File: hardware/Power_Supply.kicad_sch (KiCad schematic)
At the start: 74 parts, among them U26 LTC3122HMSE#PBF, U27 LTC3115IDHD-2#WPBF, U28 NCP1117-3.3_SOT223, U29 NCP1117-12_SOT223, U30 LM2990SX-12

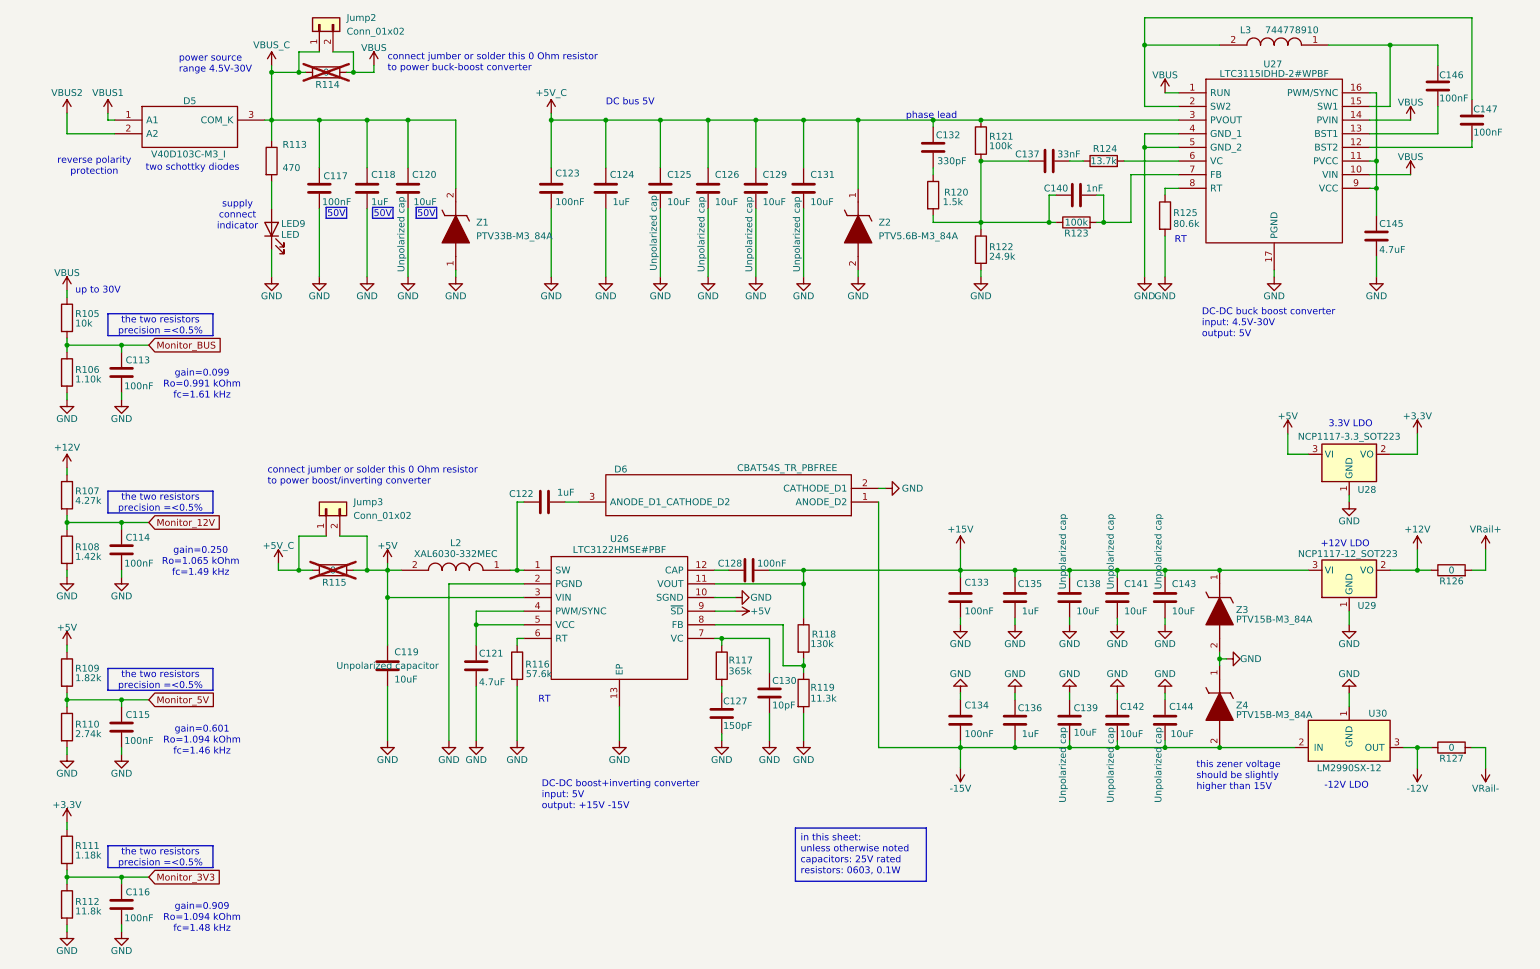
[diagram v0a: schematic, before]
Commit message: BOM for all capacitors and resistors is added correctly to the schematic
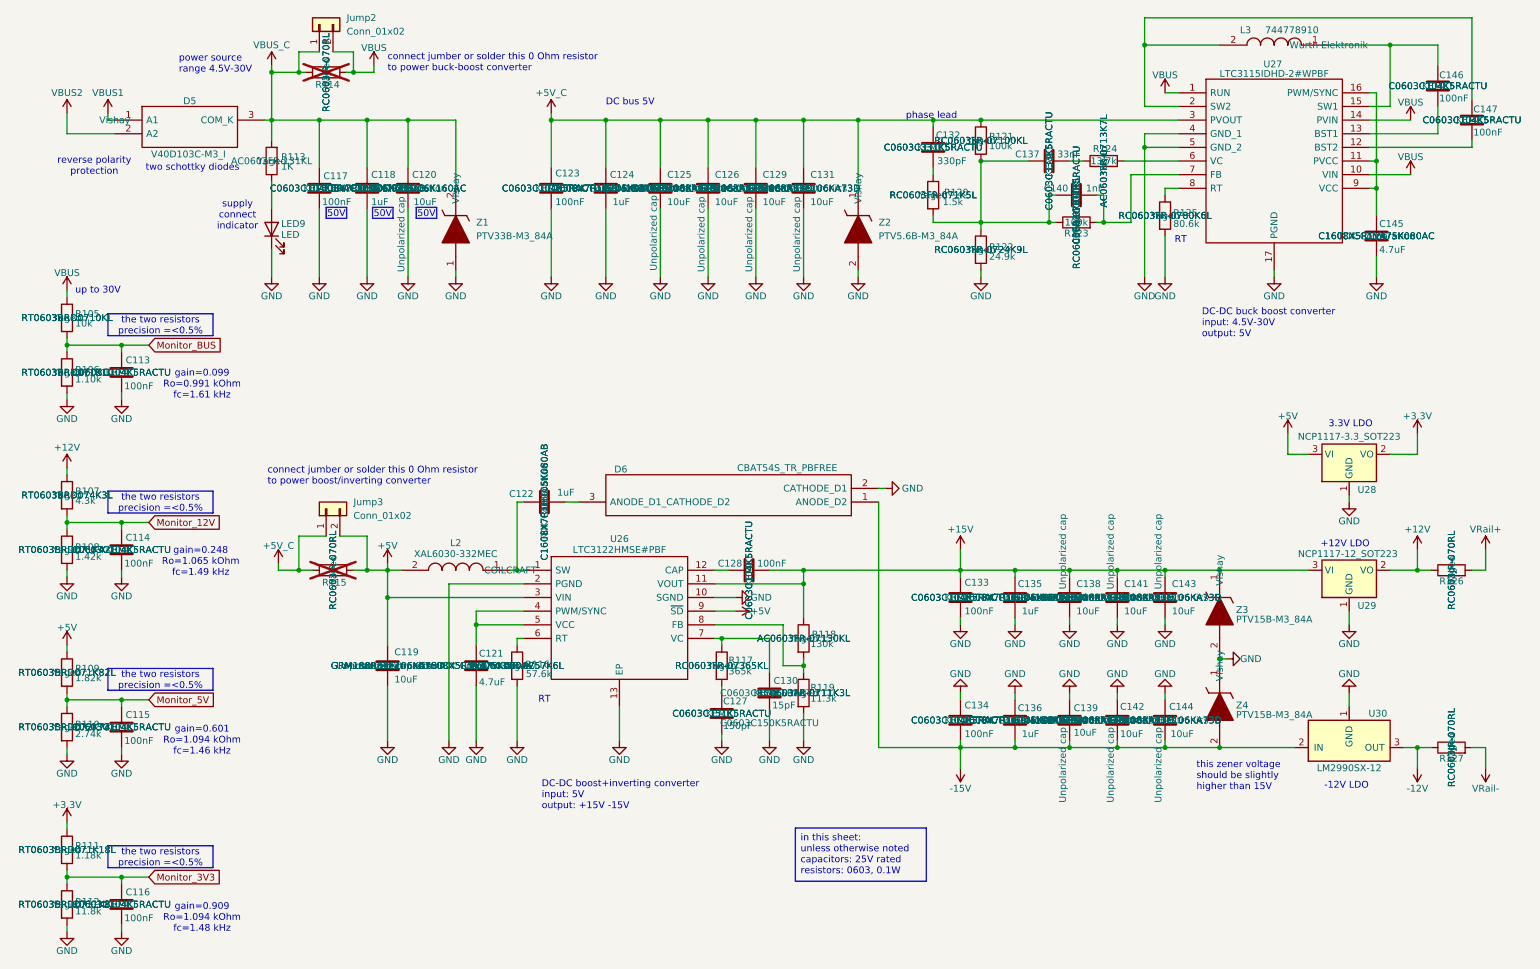
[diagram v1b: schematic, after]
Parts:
- C113, C114, C115, C116, C117, C123, C128, C133, C134, C146, C147: Link https://www.digikey.com/en/products/detail/walsin-technolog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 -> https://www.digikey.com/en/products/detail/kemet/C0603C104K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; MPN (none) -> C0603C104K5RACTU; Manufacturer Walson Technology Corporation -> KEMET; Manufacturer Number 0402B104K160CT -> (none); Manufacturer_Name (none) -> KEMET; Manufacturer_Part_Number (none) -> C0603C104K5RACTU; Rated Voltage 16V -> 50V
- C118, C122, C124, C135, C136: Link https://www.digikey.com/en/products/detail/murata-electroni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 -> https://www.digikey.com/en/products/detail/tdk-corporation/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; MPN (none) -> C1608X7R1H105K080AB; Manufacturer Murata Electronics -> TDK Corporation; Manufacturer Number GRM155R6YA105KE11J -> (none); Manufacturer_Name (none) -> TDK Corporation; Manufacturer_Part_Number (none) -> C1608X7R1H105K080AB; Rated Voltage 35V -> 50V; Tolerance (none) -> 10%
- C119, C125, C126, C129, C131, C138, C139, C141, C142, C143, C144: Link https://www.digikey.com/en/products/detail/murata-electronics/GRM21BZ71E106KE15L/13904911 -> https://www.digikey.com/en/products/detail/murata-electronics/GRM188R61E106KA73D/9867922; MPN (none) -> GRM188R61E106KA73D; Manufacturer Number GRM21BZ71E106KE15L -> (none); Manufacturer_Name (none) -> Murata Electronics; Manufacturer_Part_Number (none) -> GRM188R61E106KA73D; Tolerance (none) -> 10%
- C120: Link https://www.digikey.com/en/products/detail/murata-electroni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 -> https://www.digikey.com/en/products/detail/tdk-corporation/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; MPN (none) -> C3216X7R1H106K160AC; Manufacturer Murata Electronics -> TDK Corporation; Manufacturer Number GRM21BZ71E106KE15L -> (none); Manufacturer_Name (none) -> TDK Corporation; Manufacturer_Part_Number (none) -> C3216X7R1H106K160AC; Rated Voltage 25V -> 50V; Tolerance (none) -> 10%
- C121, C145: Link https://www.digikey.com/en/products/detail/murata-electroni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 -> https://www.digikey.com/en/products/detail/tdk-corporation/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; MPN (none) -> C1608X5R1V475K080AC; Manufacturer Murata Electronics -> TDK Corporation; Manufacturer Number GRM21BZ71E106KE15L -> (none); Manufacturer_Name (none) -> TDK Corporation; Manufacturer_Part_Number (none) -> C1608X5R1V475K080AC; Rated Voltage 25V -> 35V; Tolerance (none) -> 10%
- C127: Link https://www.digikey.com/en/products/detail/walsin-technolog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 -> https://www.digikey.com/en/products/detail/kemet/C0603C151K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; MPN (none) -> C0603C151K5RACTU; Manufacturer Walson Technology Corporation -> KEMET; Manufacturer Number 0402B104K160CT -> (none); Manufacturer_Name (none) -> KEMET; Manufacturer_Part_Number (none) -> C0603C151K5RACTU; Rated Voltage 16V -> 50V
- C130: value 10pF -> 15pF; Link https://www.digikey.com/en/products/detail/yageo/CC0402KPX7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 -> https://www.digikey.com/en/products/detail/kemet/C0603C150K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; MPN (none) -> C0603C150K5RACTU; Manufacturer Yageo -> KEMET; Manufacturer Number CC0402KPX7R8BB103 -> (none); Manufacturer_Name (none) -> KEMET; Manufacturer_Part_Number (none) -> C0603C150K5RACTU; PCBWay Link (none) -> https://www.pcbway.com/components/detail/0402B104K160CT/307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; Rated Voltage 25V -> 50V
- C132: Link https://www.digikey.com/en/products/detail/yageo/CC0402KPX7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 -> https://www.digikey.com/en/products/detail/kemet/C0603C331K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; MPN (none) -> C0603C331K5RACTU; Manufacturer Yageo -> KEMET; Manufacturer Number CC0402KPX7R8BB103 -> (none); Manufacturer_Name (none) -> KEMET; Manufacturer_Part_Number (none) -> C0603C331K5RACTU; Rated Voltage 25V -> 50V
- C137: Link https://www.digikey.com/en/products/detail/yageo/CC0402KPX7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 -> https://www.digikey.com/en/products/detail/kemet/C0603C333K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; MPN (none) -> C0603C333K5RACTU; Manufacturer Yageo -> KEMET; Manufacturer Number CC0402KPX7R8BB103 -> (none); Manufacturer_Name (none) -> KEMET; Manufacturer_Part_Number (none) -> C0603C333K5RACTU; Rated Voltage 25V -> 50V
- C140: Link https://www.digikey.com/en/products/detail/yageo/CC0402KPX7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 -> https://www.digikey.com/en/products/detail/kemet/C0603C102K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; MPN (none) -> C0603C102K5RACTU; Manufacturer Yageo -> KEMET; Manufacturer Number CC0402KPX7R8BB103 -> (none); Manufacturer_Name (none) -> KEMET; Manufacturer_Part_Number (none) -> C0603C102K5RACTU; Rated Voltage 25V -> 50V
- D5, Z1, Z2, Z3, Z4: Manufacturer (none) -> Vishay
- L2: Manufacturer (none) -> COILCRAFT
- L3: Manufacturer (none) -> Wurth Elektronik
- R105: Link https://www.digikey.com/en/products/detail/yageo/RC0402FR-0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 -> https://www.digikey.com/en/products/detail/yageo/RT0603BRD0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; MPN (none) -> RT0603BRD0710KL; Manufacturer_Name (none) -> Yageo; Manufacturer_Part_Number (none) -> RT0603BRD0710KL; Tolerance 1% -> 0.1%
- R106: Link https://www.digikey.com/en/products/detail/yageo/RC0402FR-0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 -> https://www.digikey.com/en/products/detail/yageo/RT0603BRD0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; MPN (none) -> RT0603BRD071K1L; Manufacturer_Name (none) -> Yageo; Manufacturer_Part_Number (none) -> RT0603BRD071K1L; Tolerance 1% -> 0.1%
- R107: value 4.27k -> 4.3k; Link https://www.digikey.com/en/products/detail/yageo/RC0402FR-0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 -> https://www.digikey.com/en/products/detail/yageo/RT0603BRD0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; MPN (none) -> RT0603BRD074K3L; Manufacturer_Name (none) -> Yageo; Manufacturer_Part_Number (none) -> RT0603BRD074K3L; Tolerance 1% -> 0.1%
- R108: Link https://www.digikey.com/en/products/detail/yageo/RC0402FR-0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 -> https://www.digikey.com/en/products/detail/yageo/RT0603BRD0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; MPN (none) -> RT0603BRD071K42L; Manufacturer_Name (none) -> Yageo; Manufacturer_Part_Number (none) -> RT0603BRD071K42L; Tolerance 1% -> 0.1%
- R109: Link https://www.digikey.com/en/products/detail/yageo/RC0402FR-0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 -> https://www.digikey.com/en/products/detail/yageo/RT0603BRD0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; MPN (none) -> RT0603BRD071K82L; Manufacturer_Name (none) -> Yageo; Manufacturer_Part_Number (none) -> RT0603BRD071K82L; Tolerance 1% -> 0.1%
- R110: Link https://www.digikey.com/en/products/detail/yageo/RC0402FR-0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 -> https://www.digikey.com/en/products/detail/yageo/RT0603BRD0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; MPN (none) -> RT0603BRD072K74L; Manufacturer_Name (none) -> Yageo; Manufacturer_Part_Number (none) -> RT0603BRD072K74L; Tolerance 1% -> 0.1%
- R111: Link https://www.digikey.com/en/products/detail/yageo/RC0402FR-0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 -> https://www.digikey.com/en/products/detail/yageo/RT0603BRD0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; MPN (none) -> RT0603BRD071K18L; Manufacturer_Name (none) -> Yageo; Manufacturer_Part_Number (none) -> RT0603BRD071K18L; Tolerance 1% -> 0.1%
- R112: Link https://www.digikey.com/en/products/detail/yageo/RC0402FR-0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 -> https://www.digikey.com/en/products/detail/yageo/RT0603BRD0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; MPN (none) -> RT0603BRD0711K8L; Manufacturer_Name (none) -> Yageo; Manufacturer_Part_Number (none) -> RT0603BRD0711K8L; Tolerance 1% -> 0.1%
- R113: value 470 -> 1K; Link https://www.digikey.com/en/products/detail/yageo/RC0402FR-0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 -> https://www.digikey.com/en/products/detail/yageo/AC0603FR-1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; MPN (none) -> AC0603FR-131KL; Manufacturer Number RC0402FR-07680RL -> RT0402BRD071KL; Manufacturer_Name (none) -> Yageo; Manufacturer_Part_Number (none) -> AC0603FR-131KL
- R114, R115, R126, R127: Link https://www.digikey.com/en/products/detail/yageo/RT0402BRD0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 -> https://www.digikey.com/en/products/detail/yageo/RC0603JR-0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; MPN (none) -> RC0603JR-070RL; Manufacturer_Name (none) -> Yageo; Manufacturer_Part_Number (none) -> RC0603JR-070RL; Tolerance 1% -> (none)
- R116: Link https://www.digikey.com/en/products/detail/yageo/RC0402FR-0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 -> https://www.digikey.com/en/products/detail/yageo/RC0603FR-0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; MPN (none) -> RC0603FR-0757K6L; Manufacturer_Name (none) -> Yageo; Manufacturer_Part_Number (none) -> RC0603FR-0757K6L
- R117: Link https://www.digikey.com/en/products/detail/yageo/RC0402FR-0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 -> https://www.digikey.com/en/products/detail/yageo/RC0603FR-0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; MPN (none) -> RC0603FR-07365KL; Manufacturer_Name (none) -> Yageo; Manufacturer_Part_Number (none) -> RC0603FR-07365KL
- R118: Link https://www.digikey.com/en/products/detail/yageo/RC0402FR-0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 -> https://www.digikey.com/en/products/detail/yageo/AC0603FR-0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; MPN (none) -> AC0603FR-07130KL; Manufacturer_Name (none) -> Yageo; Manufacturer_Part_Number (none) -> AC0603FR-07130KL
- R119: Link https://www.digikey.com/en/products/detail/yageo/RC0402FR-0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 -> https://www.digikey.com/en/products/detail/yageo/RC0603FR-0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; MPN (none) -> RC0603FR-0711K3L; Manufacturer_Name (none) -> Yageo; Manufacturer_Part_Number (none) -> RC0603FR-0711K3L
- R120: Link https://www.digikey.com/en/products/detail/yageo/RC0402FR-0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 -> https://www.digikey.com/en/products/detail/yageo/RC0603FR-0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; MPN (none) -> RC0603FR-071K5L; Manufacturer_Name (none) -> Yageo; Manufacturer_Part_Number (none) -> RC0603FR-071K5L
- R121: Link https://www.digikey.com/en/products/detail/yageo/RC0402FR-0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 -> https://www.digikey.com/en/products/detail/yageo/RC0603FR-0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; MPN (none) -> RC0603FR-07100KL; Manufacturer_Name (none) -> Yageo; Manufacturer_Part_Number (none) -> RC0603FR-07100KL
- R122: Link https://www.digikey.com/en/products/detail/yageo/RC0402FR-0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 -> https://www.digikey.com/en/products/detail/yageo/RC0603FR-0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; MPN (none) -> RC0603FR-0724K9L; Manufacturer_Name (none) -> Yageo; Manufacturer_Part_Number (none) -> RC0603FR-0724K9L
- R123: Link https://www.digikey.com/en/products/detail/yageo/RT0402BRD0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 -> https://www.digikey.com/en/products/detail/yageo/RC0603FR-0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; MPN (none) -> RC0603FR-07100KL; Manufacturer_Name (none) -> Yageo; Manufacturer_Part_Number (none) -> RC0603FR-07100KL
- R124: Link https://www.digikey.com/en/products/detail/yageo/RT0402BRD0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 -> https://www.digikey.com/en/products/detail/yageo/AC0603FR-0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; MPN (none) -> AC0603FR-0713K7L; Manufacturer_Name (none) -> Yageo; Manufacturer_Part_Number (none) -> AC0603FR-0713K7L
- R125: Link https://www.digikey.com/en/products/detail/yageo/RC0402FR-0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 -> https://www.digikey.com/en/products/detail/yageo/RC0603FR-0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; MPN (none) -> RC0603FR-0780K6L; Manufacturer_Name (none) -> Yageo; Manufacturer_Part_Number (none) -> RC0603FR-0780K6L
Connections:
- net VBUS_C: now also R113.2; no longer R113.1
- net at LED9.2 (A): now also R113.1; no longer R113.2
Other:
- note added: "gain=0.248 Ro=1.065 kOhm fc=1.49 kHz"
- note removed: "gain=0.250 Ro=1.065 kOhm fc=1.49 kHz"

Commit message: Not necessary text is hidden + BOM on schematic
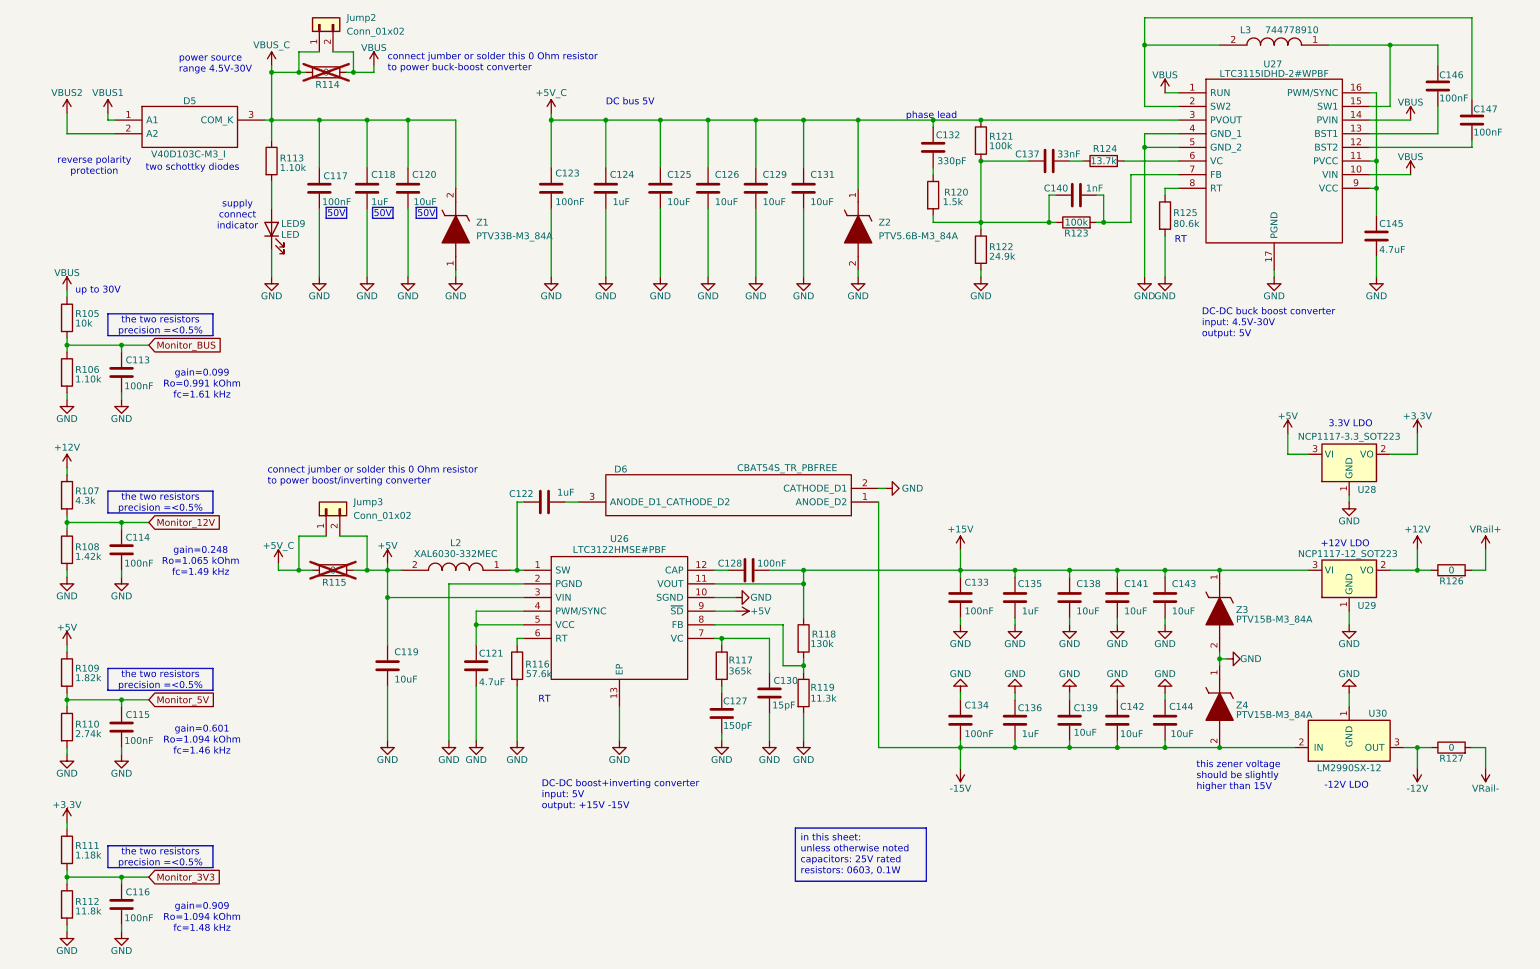
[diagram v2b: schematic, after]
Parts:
- C113, C114, C115, C116, C117, C119, C120, C121, C123, C125, C126, C127, C128, C129, C130, C131, C132, C133, C134, C137, C138, C139, C140, C141, C142, C143, C144, C145, C146, C147: Temperature Coefficient X7R -> (none)
- C118, C122, C124, C135, C136: Temperature Coefficient X5R -> (none)
- D5: MPN (none) -> V40D103C-M3/I
- D6: MPN (none) -> CBAT54S TR PBFREE
- L2: MPN (none) -> XAL6030-332MEC
- L3: MPN (none) -> 744778910
- LED9: Manufacturer_Part_Number (none) -> XZCDGK53W-1VF
- R113: value 1K -> 1.10k; Link https://www.digikey.com/en/products/detail/yageo/AC0603FR-1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 -> https://www.digikey.com/en/products/detail/yageo/RT0603BRD0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; MPN AC0603FR-131KL -> RT0603BRD071K1L; Manufacturer Number RT0402BRD071KL -> RC0402FR-07680RL; Manufacturer_Part_Number AC0603FR-131KL -> RT0603BRD071K1L; Tolerance 1% -> 0.1%
- U26: MPN (none) -> LTC3122HMSE#PBF
- U27: MPN (none) -> LTC3115IDHD-2#WPBF
- Z1: MPN (none) -> PTV33B-M3/84A
- Z2: MPN (none) -> PTV5.6B-M3/84A
- Z3, Z4: MPN (none) -> PTV15B-M3/84A
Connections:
- net VBUS_C: now also R113.1; no longer R113.2
- net at LED9.2 (A): now also R113.2; no longer R113.1

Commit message: BOM cont.
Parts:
- D5: Link (none) -> https://eu.mouser.com/ProductDetail/Vishay/V40D103C-M3-I?qs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
- D6: Link (none) -> https://www.digikey.com/en/products/detail/central-semicond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; Manufacturer (none) -> Central Semiconductor Corp
- Jump2, Jump3: Link (none) -> https://www.digikey.com/en/products/detail/harwin-inc/M20-9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; MPN (none) -> M20-9990246; Manufacturer (none) -> Harwin Inc.; Manufacturer_Name (none) -> Harwin Inc.; Manufacturer_Part_Number (none) -> M20-9990246
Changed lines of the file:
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@@
 			)
 		)
+		(property "Link" "https://www.digikey.com/en/products/detail/harwin-inc/M20-9990246/3728226"
+			(at 63.5 16.51 0)
+			(effects
+				(font
+					(size 1.27 1.27)
+				)
+				(hide yes)
+			)
+		)
+		(property "MPN" "M20-9990246"
+			(at 63.5 16.51 0)
+			(effects
+				(font
+					(size 1.27 1.27)
+				)
+				(hide yes)
+			)
+		)
+		(property "Manufacturer" "Harwin Inc."
+			(at 63.5 16.51 0)
+			(effects
+				(font
+					(size 1.27 1.27)
+				)
+				(hide yes)
+			)
+		)
+		(property "Manufacturer_Name" "Harwin Inc."
+			(at 63.5 16.51 0)
+			(effects
+				(font
+					(size 1.27 1.27)
+				)
+				(hide yes)
+			)
+		)
+		(property "Manufacturer_Part_Number" "M20-9990246"
+			(at 63.5 16.51 0)
+			(effects
+				(font
+					(size 1.27 1.27)
+				)
+				(hide yes)
+			)
+		)
 		(pin "2"
 		)
@@
 			)
 		)
+		(property "Link" "https://eu.mouser.com/ProductDetail/Vishay/V40D103C-M3-I?qs=i8QVZAFTkqRWP1GZirJttw%3D%3D"
+			(at 25.4 34.29 0)
+			(effects
+				(font
+					(size 1.27 1.27)
+				)
+				(hide yes)
+			)
+		)
 		(pin "3"
 		)
@@
 			)
 		)
+		(property "Link" "https://www.digikey.com/en/products/detail/harwin-inc/M20-9990246/3728226"
+			(at 64.77 106.68 0)
+			(effects
+				(font
+					(size 1.27 1.27)
+				)
+				(hide yes)
+			)
+		)
+		(property "MPN" "M20-9990246"
+			(at 64.77 106.68 0)
+			(effects
+				(font
+					(size 1.27 1.27)
+				)
+				(hide yes)
+			)
+		)
+		(property "Manufacturer" "Harwin Inc."
+			(at 64.77 106.68 0)
+			(effects
+				(font
+					(size 1.27 1.27)
+				)
+				(hide yes)
+			)
+		)
+		(property "Manufacturer_Name" "Harwin Inc."
+			(at 64.77 106.68 0)
+			(effects
+				(font
+					(size 1.27 1.27)
+				)
+				(hide yes)
+			)
+		)
+		(property "Manufacturer_Part_Number" "M20-9990246"
+			(at 64.77 106.68 0)
+			(effects
+				(font
+					(size 1.27 1.27)
+				)
+				(hide yes)
+			)
+		)
 		(pin "2"
 		)
@@
 			(at 167.64 105.41 0)
 			(effects
+				(font
+					(size 1.27 1.27)
+				)
+				(hide yes)
+			)
+		)
+		(property "Link" "https://www.digikey.com/en/products/detail/central-semiconductor-corp/CBAT54S-TR-PBFREE/5325130"
+			(at 167.64 105.41 0)
+			(effects
+				(font
+					(size 1.27 1.27)
+				)
+				(hide yes)
+			)
+		)
+		(property "Manufacturer" "Central Semiconductor Corp"
+			(at 167.64 105.41 0)
+			(effects

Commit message: TVS16,TVS17,TVS18,TVS19 parts have been changed from ESDSB12VLB-TP to PESD12VL1BSLAZ
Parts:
- Z1, Z3, Z4: footprint PTV47BM384A -> harp.device.quad.dac.kicad:PTV47BM384A
- Z2: footprint PTV56BM384A -> harp.device.quad.dac.kicad:PTV47BM384A
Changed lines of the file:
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@@
 			)
 		)
-		(property "Footprint" "PTV47BM384A"
+		(property "Footprint" "harp.device.quad.dac.kicad:PTV47BM384A"
 			(at 234.95 128.27 0)
 			(effects
@@
 			)
 		)
-		(property "Footprint" "PTV47BM384A"
+		(property "Footprint" "harp.device.quad.dac.kicad:PTV47BM384A"
 			(at 92.71 57.15 0)
 			(effects
@@
 			)
 		)
-		(property "Footprint" "PTV56BM384A"
+		(property "Footprint" "harp.device.quad.dac.kicad:PTV47BM384A"
 			(at 167.64 57.15 0)
 			(effects
@@
 			)
 		)
-		(property "Footprint" "PTV47BM384A"
+		(property "Footprint" "harp.device.quad.dac.kicad:PTV47BM384A"
 			(at 234.95 146.05 0)
 			(effects

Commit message: The layout is complete, and the design is currently in the review stage.
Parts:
- Z1: symbol PTV33B-M3_84A:PTV33B-M3_84A -> harp.device.quad.dac:PTV15B-M3_84A
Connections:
- net GND: now also Z1.2 (A); no longer Z1.1
- net VBUS_C: now also Z1.1 (K); no longer Z1.2
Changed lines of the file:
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@@
 	)
 	(symbol
-		(lib_id "PTV33B-M3_84A:PTV33B-M3_84A")
+		(lib_id "harp.device.quad.dac:PTV15B-M3_84A")
 		(at 88.9 46.99 270)
 		(unit 1)

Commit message: Continue BOM + enhance BOM + enhance schematic
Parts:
- C118, C120, C121, C122, C124, C135, C136, C145: Manufacturer TDK Corporation -> TDK; Manufacturer_Name TDK Corporation -> TDK
- Jump2, Jump3: Manufacturer Harwin Inc. -> Harwin; Manufacturer_Name Harwin Inc. -> Harwin
- L2: Link (none) -> https://www.digikey.com/en/products/detail/coilcraft/XAL603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
- L3: Link (none) -> https://www.digikey.com/en/products/detail/w%C3%BCrth-elekt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
- LED9: Manufacturer_Name (none) -> SunLED
- U26, U27: Link (none) -> https://www.digikey.com/en/products/detail/analog-devices-i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; Manufacturer (none) -> Analog Devices
- U28: value NCP1117-3.3_SOT223 -> NCV1117ST33T3G; Link (none) -> https://www.digikey.com/en/products/detail/onsemi/NCV1117ST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; MPN (none) -> NCV1117ST33T3G; Manufacturer (none) -> Onsemi; Manufacturer_Name (none) -> Onsemi; Manufacturer_Part_Number (none) -> NCV1117ST33T3G
- U29: value NCP1117-12_SOT223 -> NCV1117ST12T3G; Link (none) -> https://www.digikey.com/en/products/detail/onsemi/NCV1117ST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; MPN (none) -> NCV1117ST12T3G; Manufacturer (none) -> Onsemi; Manufacturer_Name (none) -> Onsemi; Manufacturer_Part_Number (none) -> NCV1117ST12T3G
- U30: value LM2990SX-12 -> LM2990S-12/NOPB; Link (none) -> https://www.digikey.com/en/products/detail/texas-instrument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; MPN (none) -> LM2990S-12/NOPB; Manufacturer (none) -> Texas Instruments; Manufacturer_Name (none) -> Texas Instruments; Manufacturer_Part_Number (none) -> LM2990S-12/NOPB
- Z1, Z2, Z3, Z4: Link (none) -> https://www.digikey.com/en/products/detail/vishay-general-s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
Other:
- note added: "10uH, 1.83A"
- note added: "3.3uH, 8A"
- note added: "Yellow"
